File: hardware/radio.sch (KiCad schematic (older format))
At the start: 86 parts, among them J1 JCLK, U1 G144A12, U3V3t1V8 NCP1117ST18T3G, U5V0t3V3 NCP1117ST33T3G

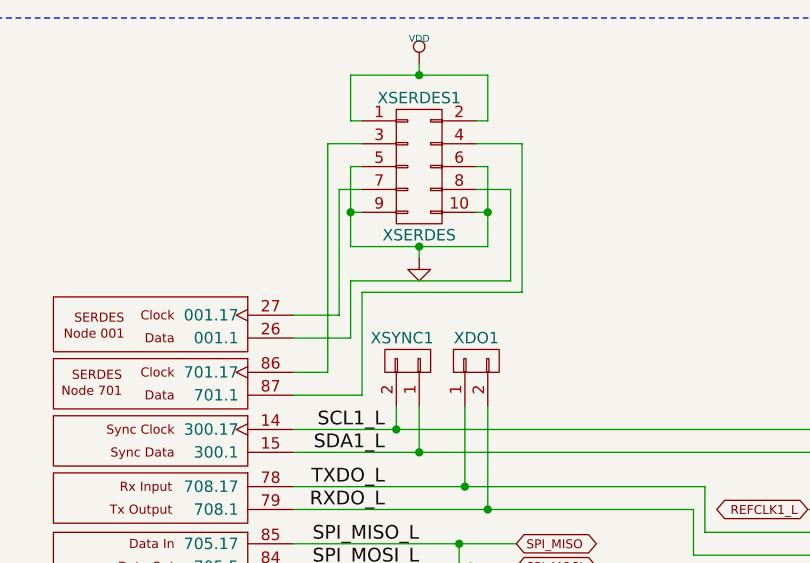
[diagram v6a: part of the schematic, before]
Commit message: Removing the XSERDES1 header.
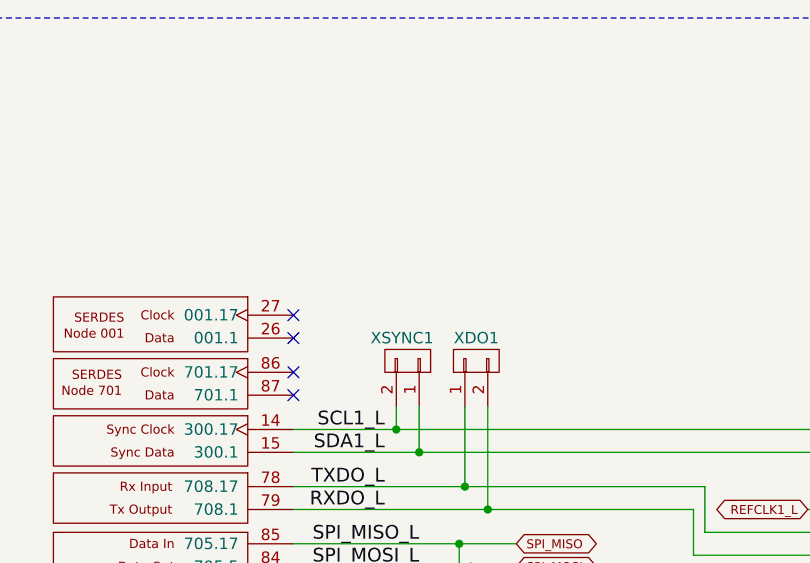
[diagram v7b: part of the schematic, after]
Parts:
- removed XSERDES1: XSERDES, Pin_Headers:Pin_Header_Straight_2x05, symbol CONN_02X05
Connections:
- wire segments 512 -> 482
- no-connect marks 3 -> 7
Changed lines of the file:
@@
 Text Notes 13800 4050 2    60   ~ 0
 RPI Hat ID EEPROM
-$Comp
-L CONN_02X05 XSERDES1
-U 1 1 54187398
-P 2400 1200
-F 0 "XSERDES1" H 2400 1500 50  0000 C CNN
-F 1 "XSERDES" H 2400 900 50  0000 C CNN
-F 2 "Pin_Headers:Pin_Header_Straight_2x05" H 2400 0   60  0001 C CNN
-F 3 "" H 2400 0   60  0000 C CNN
-	1    2400 1200
-	1    0    0    -1
-$EndComp
-$Comp
-L VDD #PWR016
-U 1 1 54189E40
-P 2400 750
-F 0 "#PWR016" H 2400 850 30  0001 C CNN
-F 1 "VDD" H 2400 860 30  0000 C CNN
-F 2 "" H 2400 750 60  0000 C CNN
-F 3 "" H 2400 750 60  0000 C CNN
-	1    2400 750
-	1    0    0    -1
-$EndComp
-$Comp
-L GND #PWR017
-U 1 1 54189E88
-P 2400 1600
-F 0 "#PWR017" H 2400 1600 30  0001 C CNN
-F 1 "GND" H 2400 1530 30  0001 C CNN
-F 2 "" H 2400 1600 60  0000 C CNN
-F 3 "" H 2400 1600 60  0000 C CNN
-	1    2400 1600
-	1    0    0    -1
-$EndComp
 Text Label 6400 2700 2    60   ~ 0
 REFCLK1_H
@@
 Connection ~ 12050 4050
 Wire Wire Line
-	2150 1400 2100 1400
-Wire Wire Line
-	2100 1200 2100 1550
-Wire Wire Line
-	2100 1550 2700 1550
-Wire Wire Line
-	2700 1550 2700 1200
-Wire Wire Line
-	2700 1400 2650 1400
-Wire Wire Line
-	2700 1200 2650 1200
-Connection ~ 2700 1400
-Wire Wire Line
-	2150 1200 2100 1200
-Connection ~ 2100 1400
-Wire Wire Line
-	2150 2200 1850 2200
-Wire Wire Line
-	2150 1750 2150 2200
-Wire Wire Line
-	2150 1750 2850 1750
-Wire Wire Line
-	2850 1750 2850 1100
-Wire Wire Line
-	2850 1100 2650 1100
-Wire Wire Line
-	1850 1950 2100 1950
-Wire Wire Line
-	2100 1950 2100 1700
-Wire Wire Line
-	2100 1700 2800 1700
-Wire Wire Line
-	2800 1700 2800 1300
-Wire Wire Line
-	2800 1300 2650 1300
-Wire Wire Line
-	1850 2100 2000 2100
-Wire Wire Line
-	2000 2100 2000 1100
-Wire Wire Line
-	2000 1100 2150 1100
-Wire Wire Line
-	1850 1850 2050 1850
-Wire Wire Line
-	2050 1850 2050 1300
-Wire Wire Line
-	2050 1300 2150 1300
-Wire Wire Line
-	2150 1000 2100 1000
-Wire Wire Line
-	2100 1000 2100 800
-Wire Wire Line
-	2100 800  2700 800
-Wire Wire Line
-	2700 800  2700 1000
-Wire Wire Line
-	2700 1000 2650 1000
-Wire Wire Line
-	2400 800  2400 750
-Connection ~ 2400 800
-Wire Wire Line
-	2400 1600 2400 1550
-Connection ~ 2400 1550
-Wire Wire Line
 	28275 7550 28275 7500
 Wire Wire Line
@@
 Wire Wire Line
 	30425 5950 30425 6450
+NoConn ~ 1850 1850
+NoConn ~ 1850 1950
+NoConn ~ 1850 2100
+NoConn ~ 1850 2200
 $EndSCHEMATC

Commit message: Getting close to first production run.
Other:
- moved on the sheet: AN0, AN1, AN2, AT0, C1, C2, C3, C4, C5, C6, C7, C8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
